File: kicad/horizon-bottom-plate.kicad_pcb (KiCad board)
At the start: 2 copper layers, 266 x 76 mm, 54 parts, among them J1 OLED, SW1 SW_Push, SW10 SW_Push, SW11 SW_Push, SW12 SW_Push, SW13 SW_Push, SW14 SW_Push, SW15 SW_Push, SW16 SW_Push, SW17 SW_Push, SW18 SW_Push, SW19 SW_Push, SW2 SW_Push, SW20 SW_Push, SW21 SW_Push, SW22 SW_Push, SW23 SW_Push, SW24 SW_Push, SW25 SW_Push, SW26 SW_Push, SW27 SW_Push, SW28 SW_Push, SW29 SW_Push, SW3 SW_Push, SW30 SW_Push, SW31 SW_Push, SW32 SW_Push, SW33 SW_Push, SW34 SW_Push, SW35 SW_Push, SW36 SW_Push, SW37 SW_Push, SW38 SW_Push, SW39 SW_Push, SW4 SW_Push, SW40 SW_Push, SW41 SW_Push, SW42 SW_Push, SW5 SW_Push, SW6 SW_Push, SW7 SW_Push, SW8 SW_Push, SW9 SW_Push, U1 PRO-MICRO

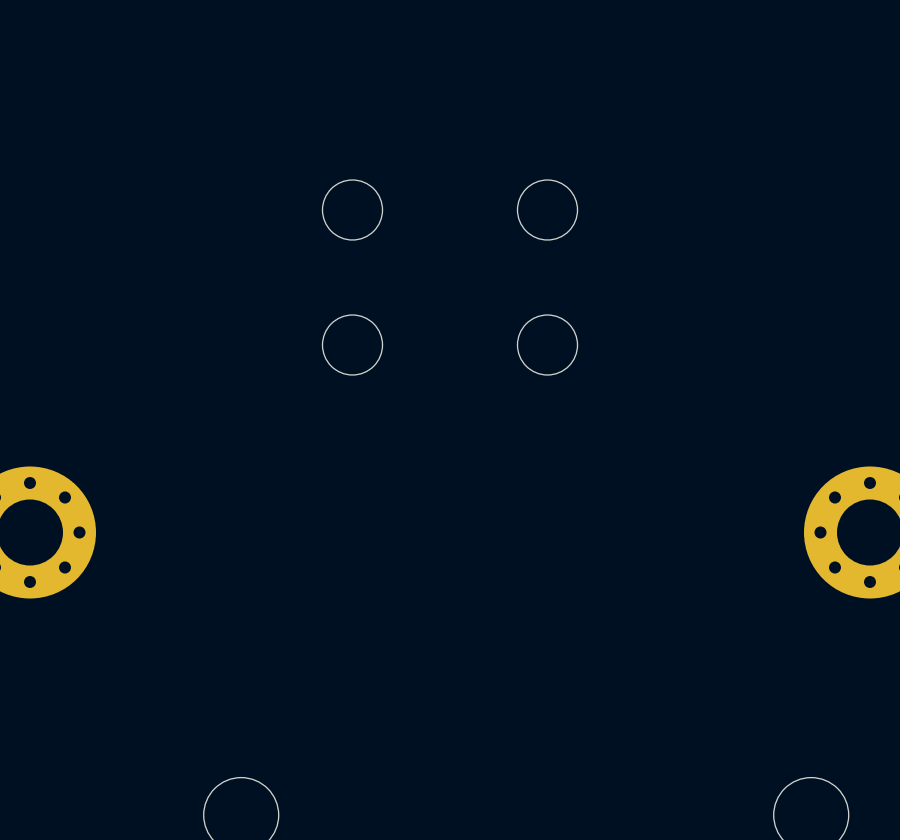
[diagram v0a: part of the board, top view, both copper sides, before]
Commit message: Adjust center component layout for MX and Choc consistency.
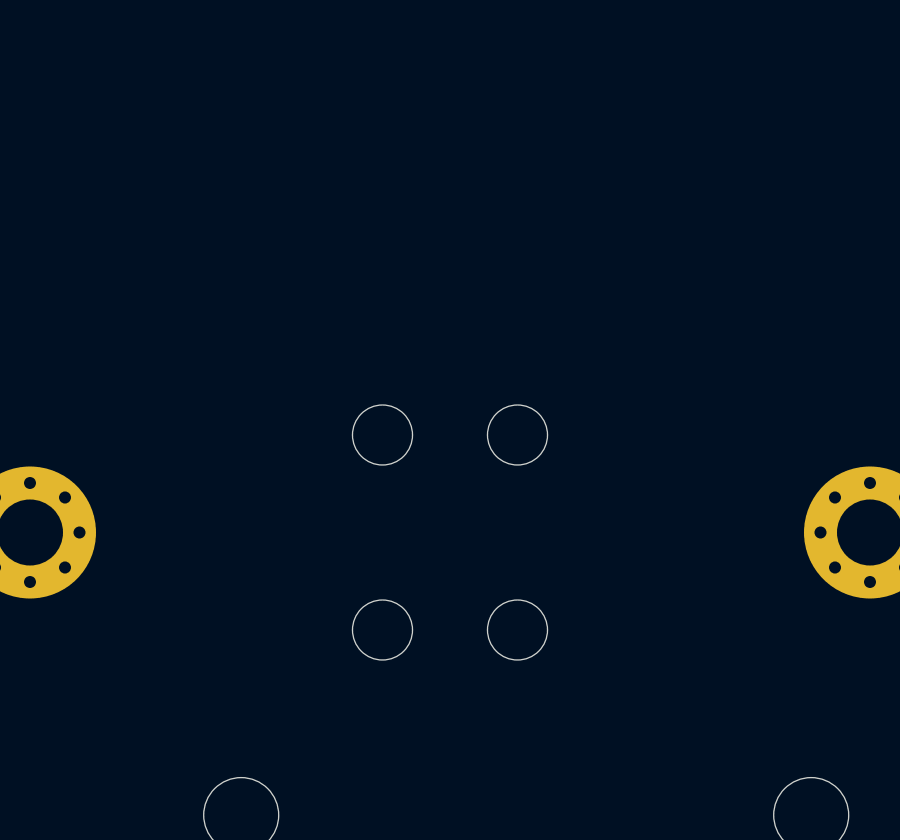
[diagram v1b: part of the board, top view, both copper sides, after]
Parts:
- moved TSW1 8.50 mm to (209.0, 147.0), turned to 90 degrees
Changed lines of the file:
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@@
   )
   (module horizon-footprints:Cutout-SW_Push_6mm (layer F.Cu)
-    (at 209 138.5)
+    (at 209 147 90)
     (descr "Cutout fox 6mmx6mm push button")
     (tags Cutout)
-    (fp_text reference TSW1 (at 0 0) (layer F.SilkS) hide
+    (fp_text reference TSW1 (at 0 0 90) (layer F.SilkS) hide
       (effects (font (size 1 1) (thickness 0.15)))
     )
-    (fp_text value RESET (at 0 4) (layer F.Fab)
+    (fp_text value RESET (at 0 4 90) (layer F.Fab)
       (effects (font (size 1 1) (thickness 0.15)))
     )
@@
     (fp_line (start 3 -3) (end 3 3) (layer F.Fab) (width 0.1))
     (fp_line (start 0 -3) (end 3 -3) (layer F.Fab) (width 0.1))
-    (pad "" np_thru_hole circle (at 3.25 -2.25) (size 2 2) (drill 2) (layers *.Cu *.Mask))
-    (pad "" np_thru_hole circle (at 3.25 2.25) (size 2 2) (drill 2) (layers *.Cu *.Mask))
-    (pad "" np_thru_hole circle (at -3.25 -2.25) (size 2 2) (drill 2) (layers *.Cu *.Mask))
-    (pad "" np_thru_hole circle (at -3.25 2.25) (size 2 2) (drill 2) (layers *.Cu *.Mask))
+    (pad "" np_thru_hole circle (at 3.25 -2.25 90) (size 2 2) (drill 2) (layers *.Cu *.Mask))
+    (pad "" np_thru_hole circle (at 3.25 2.25 90) (size 2 2) (drill 2) (layers *.Cu *.Mask))
+    (pad "" np_thru_hole circle (at -3.25 -2.25 90) (size 2 2) (drill 2) (layers *.Cu *.Mask))
+    (pad "" np_thru_hole circle (at -3.25 2.25 90) (size 2 2) (drill 2) (layers *.Cu *.Mask))
   )
   (module horizon-footprints:Cutout-Header_1x04_2.54mm (layer F.Cu)
